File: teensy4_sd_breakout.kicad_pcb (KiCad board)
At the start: 2 copper layers, 17.8 x 22.9 mm, 3 parts, among them J1 Conn_01x09, J2 Micro_SD_Card_Det

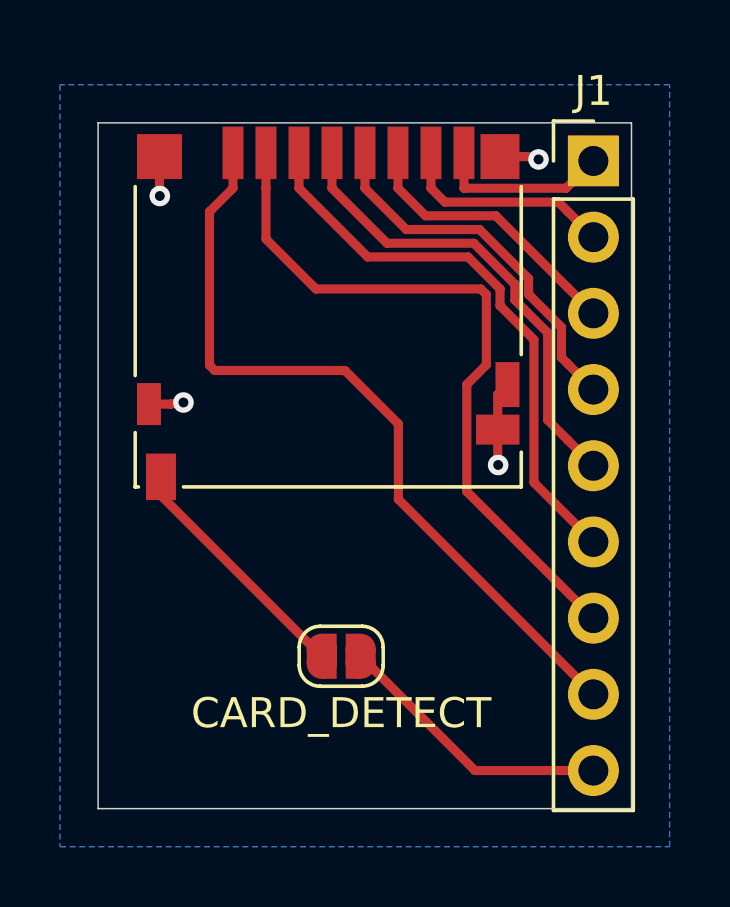
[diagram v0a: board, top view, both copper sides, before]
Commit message: Added decoupling cap and back silk screen
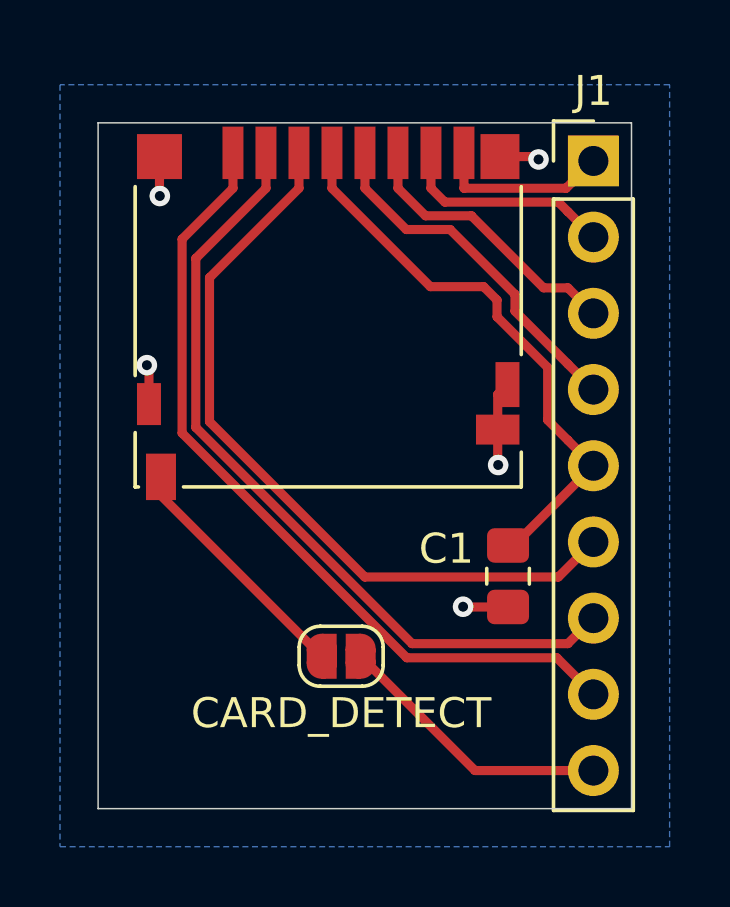
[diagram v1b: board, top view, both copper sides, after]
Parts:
- added C1: C_Small, Capacitor_SMD:C_0805_2012Metric_Pad1.15x1.40mm_HandSolder, F.Cu at (136.9, 95.1)
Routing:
- net /CMD: track 19.0 -> 25.6 mm
- net /3V3: track 15.7 -> 19.0 mm
- net /DAT3: track 23.8 -> 26.7 mm
- net /GND: track 16.0 -> 17.7 mm, vias 4 -> 5
- net /DAT2: track 26.2 -> 27.4 mm
- net /CLK: track 12.5 -> 11.9 mm
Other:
- board text added: "DAT1 DAT0 GND CLK 3V3 CMD DAT3 DAT2 CD/29"
- board text added: "Teensy 4.0 SD breakout 2019-09-24"

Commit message: Updated documentation and silkscreen
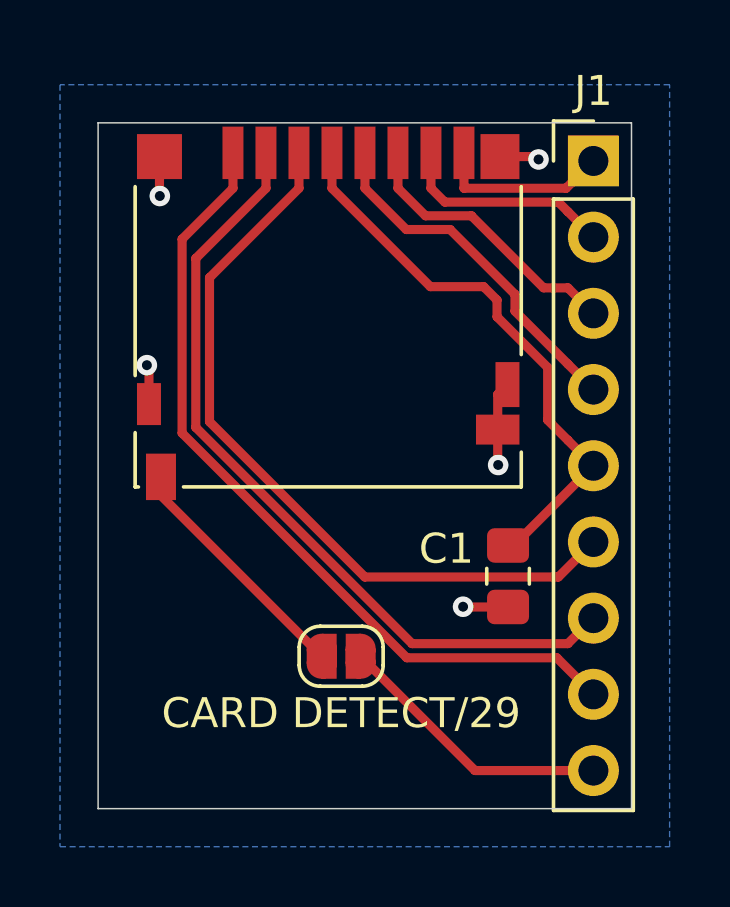
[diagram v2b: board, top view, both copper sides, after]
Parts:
- C1: value C_Small -> 0.1u
- JP1: value CARD_DETECT -> CARD DETECT/29
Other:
- board text added: "Teensy 4.0 SD breakout 2019-10-05"
- board text removed: "Teensy 4.0 SD breakout 2019-09-24"
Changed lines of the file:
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@@
   )
   (setup
-    (last_trace_width 0.3048)
+    (last_trace_width 0.1524)
     (user_trace_width 0.1524)
     (user_trace_width 0.3048)
@@
       (effects (font (size 1 1) (thickness 0.15)))
     )
-    (fp_text value C_Small (at 0 1.65 90) (layer F.Fab)
+    (fp_text value 0.1u (at 0 1.65 90) (layer F.Fab)
       (effects (font (size 1 1) (thickness 0.15)))
     )
@@
       (effects (font (size 1 1) (thickness 0.15)))
     )
-    (fp_text value CARD_DETECT (at 0 1.9) (layer F.SilkS)
+    (fp_text value "CARD DETECT/29" (at 0 1.9) (layer F.SilkS)
       (effects (font (size 1 1) (thickness 0.15)))
     )
@@
     (effects (font (size 1.5 1.5) (thickness 0.3)) (justify left mirror))
   )
-  (gr_text "Teensy 4.0\nSD breakout\n2019-09-24" (at 127.381 91.567 90) (layer B.SilkS)
+  (gr_text "Teensy 4.0\nSD breakout\n2019-10-05" (at 127.381 91.567 90) (layer B.SilkS)
     (effects (font (size 1.5 1.5) (thickness 0.3)) (justify mirror))
   )
